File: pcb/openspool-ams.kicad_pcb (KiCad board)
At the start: 2 copper layers, 30.5 x 58.4 mm, 9 parts, among them J1 GND, J2 ESP32-L, J3 ESP32-R, J4 5V, J5 MOSI, J6 CS, J7 3V3, J8 SCK, J9 MISO

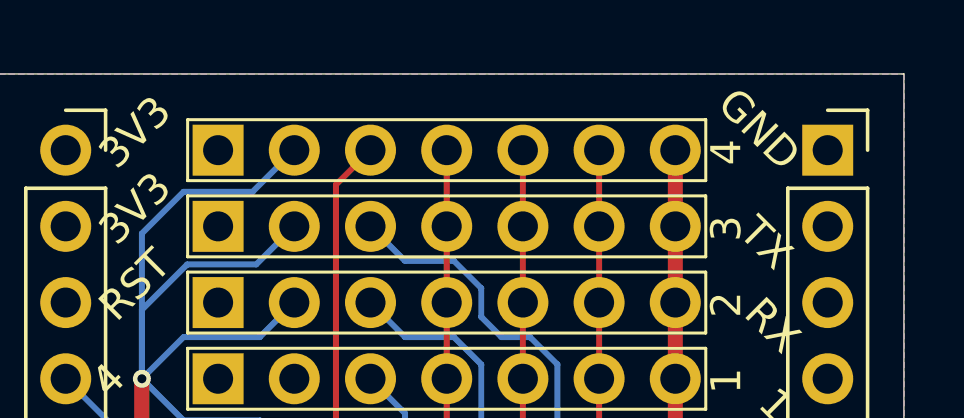
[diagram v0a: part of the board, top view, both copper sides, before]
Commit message: Added hints to silkscreen
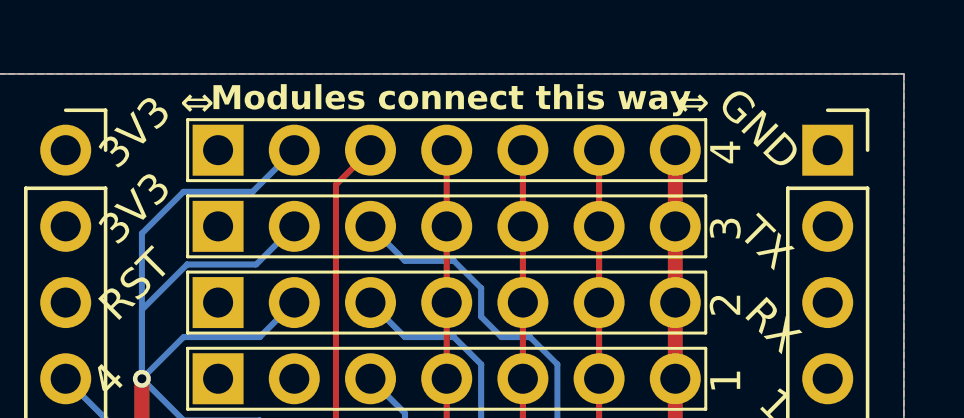
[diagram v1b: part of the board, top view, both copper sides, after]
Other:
- board text added: "Modules connect this way"
- board text added: "⇔"
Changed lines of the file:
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@@
 		(sheetname "/")
 		(sheetfile "openspool-ams.kicad_sch")
-		(attr through_hole)
+		(attr through_hole dnp)
 		(fp_line
 			(start 1.27 0.635)
@@
 		(sheetname "/")
 		(sheetfile "openspool-ams.kicad_sch")
-		(attr through_hole)
+		(attr through_hole dnp)
 		(fp_line
 			(start 1.27 0.635)
@@
 		(sheetname "/")
 		(sheetfile "openspool-ams.kicad_sch")
-		(attr through_hole)
+		(attr through_hole dnp)
 		(fp_line
 			(start 1.27 0.635)
@@
 		(sheetname "/")
 		(sheetfile "openspool-ams.kicad_sch")
-		(attr through_hole)
+		(attr through_hole dnp)
 		(fp_line
 			(start 1.27 0.635)
@@
 		(sheetname "/")
 		(sheetfile "openspool-ams.kicad_sch")
-		(attr through_hole)
+		(attr through_hole dnp)
 		(fp_line
 			(start 1.27 0.635)
@@
 		(sheetname "/")
 		(sheetfile "openspool-ams.kicad_sch")
-		(attr through_hole)
+		(attr through_hole dnp)
 		(fp_line
 			(start 1.27 0.635)
@@
 		(sheetname "/")
 		(sheetfile "openspool-ams.kicad_sch")
-		(attr through_hole)
+		(attr through_hole dnp)
 		(fp_line
 			(start 1.27 0.635)
@@
 		)
 	)
+	(gr_text "⇔"
+		(at 69.85 49.784 0)
+		(layer "F.SilkS")
+		(effects
+			(font
+				(size 1 1)
+				(thickness 0.1)
+			)
+			(justify left bottom)
+		)
+	)
 	(gr_text "36"
 		(at 90.424 79.502 315)
@@
 		)
 	)
+	(gr_text "⇔"
+		(at 86.36 49.784 0)
+		(layer "F.SilkS")
+		(effects
+			(font
+				(size 1 1)
+				(thickness 0.1)
+			)
+			(justify left bottom)
+		)
+	)
 	(gr_text "39"
 		(at 90.424 71.882 315)
@@
 			)
 			(justify right top)
+		)
+	)
+	(gr_text "Modules connect this way"
+		(at 70.866 49.53 0)
+		(layer "F.SilkS")
+		(effects
+			(font
+				(size 0.8 0.8)
+				(thickness 0.16)
+				(bold yes)
+			)
+			(justify left bottom)
 		)
 	)
@@
 		)
 	)
+	(gr_text "Modules connect this way"
+		(at 86.614 49.53 0)
+		(layer "B.SilkS")
+		(effects
+			(font
+				(size 0.8 0.8)
+				(thickness 0.1)
+			)
+			(justify left bottom mirror)
+		)
+	)
 	(gr_text "3V3"
 		(at 67.818 50.038 315)
@@
 			)
 			(justify right top mirror)
+		)
+	)
+	(gr_text "⇔"
+		(at 69.85 48.725 180)
+		(layer "B.SilkS")
+		(effects
+			(font
+				(size 1 1)
+				(thickness 0.1)
+			)
+			(justify left bottom mirror)
 		)
 	)
@@
 		)
 	)
+	(gr_text "⇔"
+		(at 86.36 48.725 180)
+		(layer "B.SilkS")
+		(effects
+			(font
+				(size 1 1)
+				(thickness 0.1)
+			)
+			(justify left bottom mirror)
+		)
+	)
